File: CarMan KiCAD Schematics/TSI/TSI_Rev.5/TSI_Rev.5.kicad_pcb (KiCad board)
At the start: 2 copper layers, 203.2 x 165.1 mm, 266 parts, among them IC1 TS431ILT, IC4 TS431ILT, J1 TSV, J10 Breakered GLV, J11 Dashboard/EPAL, J12 Battery Packs SL, J13 RSP Safety Loop, J14.1 Logic Conn. 1, J14.2 Logic Conn. 2, J15 Roll Hoop TSAL, J16 Throttle Plau., J17 Brakes & BOT SL, J18 RTDS & Brk Light, J19 Cooling Sensors, J2 Current_Sensor, J20 IMD & AMS BTN, J21 Left Test Conn., J22 Right Side Conn., J23 I2C, J24 MC+ Short Pin 1, J25 MC+ Short Pin 2, J26 HV+ Short Pin 1, J27 HV+ Short Pin 2, J28 HV- Short Pin 1, J29 HV- Short Pin 2, J3 MC, J30 GLV Hook-up Pin, J31 Cooling Jumper, J4 PC Relay, J5 DC Relay, J6 IMD, J7 BP Can & Power, J8 Cockpit, J9 Cooling Power, K1 APAN3105, K2 G5LE-1-E, K3 SFS2-DC24V, K4 SFS2-DC24V, Q1 ZVP1320F, Q11 TN2130K1-G, Q2 MMBF170, Q3 ZVP1320F, Q5 SI1302DL-T1-E3, SW1 TS5A3159DBVT, U1 RDE03110S12, U10 MC7805BDTRKG, U11 TLP293, U12 REF3033, U13 TLP293, U14 Bottom Left, U15 Top Left, U16 TS372CDT, U17 Top Right, U18 MCP6004, U19 74HC00, U2 Bottom Right, U20 TLP293, U21 MCP6004, U22 MCP23016-I_SO, U23 DAC5574IDGS, U24 TLP293, U25 NCD9830DBR2G, U26 MCP6004, U29 SN74LVC1G08DCKR, U3 TS912, U30 TLP293, U31 TLP293, U32 TLP293, U34 TLP293, U35 MCP6004, U37 TLP293, U4 ACPL-C870, U40 MCP6004, U41 PDQ10-Q24-D5-D, U42 LT1763CS8-3.3PBF, U48 TLP293, U49 TLP293, U5 SI8600AB-B-IS, U6 TS912, U7 MCP6004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

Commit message: Updated Brake_Pressed_uC Signal
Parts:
- added R98: 1k, Resistor_SMD:R_0805_2012Metric_Pad1.15x1.40mm_HandSolder, F.Cu at (200.7, 40.6)
- added TP15: SL1_IMD_Out, TestPoint:TestPoint_Pad_D3.0mm, F.Cu at (157.0, 46.5)
- added TP16: SL1_AMS_Out, TestPoint:TestPoint_Pad_D3.0mm, F.Cu at (162.0, 46.5)
- C13: footprint Capacitor_SMD:CP_Elec_10x10 -> Capacitor_THT:CP_Radial_D8.0mm_P3.50mm
- moved C13 0.66 mm to (124.4, 137.2)
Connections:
- U30 pad 3: /AIRS- -> /Throttle_Plausibility/Brake_Pressed_uC
- U30 pad 4: /Throttle_Plausibility/Brake_Pressed_uC -> /Throttle_Plausibility/3.3V

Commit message: TSI Updated & error fixes: added pull down resistors, and 5V_ISO_RTN
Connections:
- IC1 pad 1: Net-(IC1-Pad1) -> (no net)
- IC1 pad 2: Net-(IC1-Pad2) -> (no net)
- IC4 pad 1: Net-(IC4-Pad1) -> (no net)
- IC4 pad 2: Net-(IC4-Pad2) -> (no net)
- J11 pad 8: Net-(J11-Pad8) -> (no net)
- J13 pad 4: Net-(J13-Pad4) -> (no net)
- J2 pad 1: Net-(J2-Pad1) -> (no net)
- J2 pad 6: Net-(J2-Pad6) -> (no net)
- J3 pad 4: Net-(J3-Pad4) -> (no net)
- J6 pad 6: Net-(J6-Pad6) -> (no net)
- J6 pad 7: Net-(J6-Pad7) -> (no net)
- J8 pad 4: Net-(J8-Pad4) -> (no net)
- K2 pad 3: Net-(K2-Pad3) -> (no net)
- K3 pad 3: Net-(K3-Pad3) -> (no net)
- K3 pad 4: Net-(K3-Pad4) -> (no net)
- K4 pad 3: Net-(K4-Pad3) -> (no net)
- K4 pad 4: Net-(K4-Pad4) -> (no net)
- PS1 pad 4: Net-(PS1-Pad4) -> (no net)
- PS1 pad 6: Net-(PS1-Pad6) -> (no net)
- PS2 pad 5: Net-(PS2-Pad5) -> (no net)
- PS2 pad 6: Net-(PS2-Pad6) -> (no net)
- PS2 pad 7: Net-(PS2-Pad7) -> (no net)
- R83 pad 2: /Relays_Cooling_Voltage_Refs/MRSET_Contact -> (no net)
- RV5 pad 3: Net-(RV5-Pad3) -> (no net)
- U22 pad 26: Net-(U22-Pad26) -> (no net)
- U22 pad 27: Net-(U22-Pad27) -> (no net)
- U22 pad 28: Net-(U22-Pad28) -> (no net)
- U22 pad 6: Net-(U22-Pad6) -> (no net)
- U23 pad 2: Net-(U23-Pad2) -> (no net)
- U23 pad 4: Net-(U23-Pad4) -> (no net)
- U23 pad 5: Net-(U23-Pad5) -> (no net)
- U25 pad 1: Net-(U25-Pad1) -> (no net)
- U25 pad 2: Net-(U25-Pad2) -> (no net)
- U25 pad 3: Net-(U25-Pad3) -> (no net)
- U25 pad 6: Net-(U25-Pad6) -> (no net)
- U30 pad 4: /Throttle_Plausibility/3.3V -> (no net)
- U41 pad 6: Net-(U41-Pad6) -> (no net)
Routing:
- net /24V_BP_Out: track 75.4 -> 0.00 mm
- net /SL1_In: track 133.5 -> 105.5 mm
- net /AIRS+: track 96.8 -> 123.7 mm
- net /AIRS-: track 347.7 -> 321.9 mm
- net /IMD_Status: track 231.6 -> 208.2 mm
- net /Throttle_HV: track 137.1 -> 121.0 mm
- net /24V: track 800.3 -> 787.6 mm
- net /BRAKE_OUT: track 218.5 -> 208.4 mm
- net /Gen_Fault_EPAL: track 145.3 -> 137.3 mm
- net /Relays_Cooling_Voltage_Refs/SR_CTRL_Boosted: track 72.2 -> 67.0 mm
- net /Drive_BTN: track 92.1 -> 88.6 mm
- net /BOT_Out: track 66.5 -> 63.5 mm
- net Net-(J3-Pad7): track 29.3 -> 26.9 mm
- net /Brake_Pressed_HV: track 42.8 -> 40.4 mm
- net /5V: track 541.8 -> 540.0 mm
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
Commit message: Updated D2 Footprint
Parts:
- added R99: 1K, Resistor_SMD:R_0805_2012Metric_Pad1.15x1.40mm_HandSolder, F.Cu at (141.2, 41.9)
- D2: footprint Package_SO:MSOP-8_3x3mm_P0.65mm -> Package_SO:SO-8_5.3x6.2mm_P1.27mm
- R61: value 960 -> 1K
- R98: value 1k -> 1K
- moved D1 155.0 mm to (136.4, 41.9)
- moved D4 148.9 mm to (149.9, 41.9), turned to 0 degrees
- moved D2 34.4 mm to (125.7, 45.7)
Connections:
- U11 pad 2: /AIRS- -> /5V_ISO_RTN
- U13 pad 2: /AIRS- -> /5V_ISO_RTN
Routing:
- net Net-(Q2-Pad3): track 134.9 -> 122.4 mm
- net /AIRS-: track 321.9 -> 312.1 mm
- net /Throttle_Plausibility/APPS2_b: track 100.4 -> 95.0 mm, vias 7 -> 6

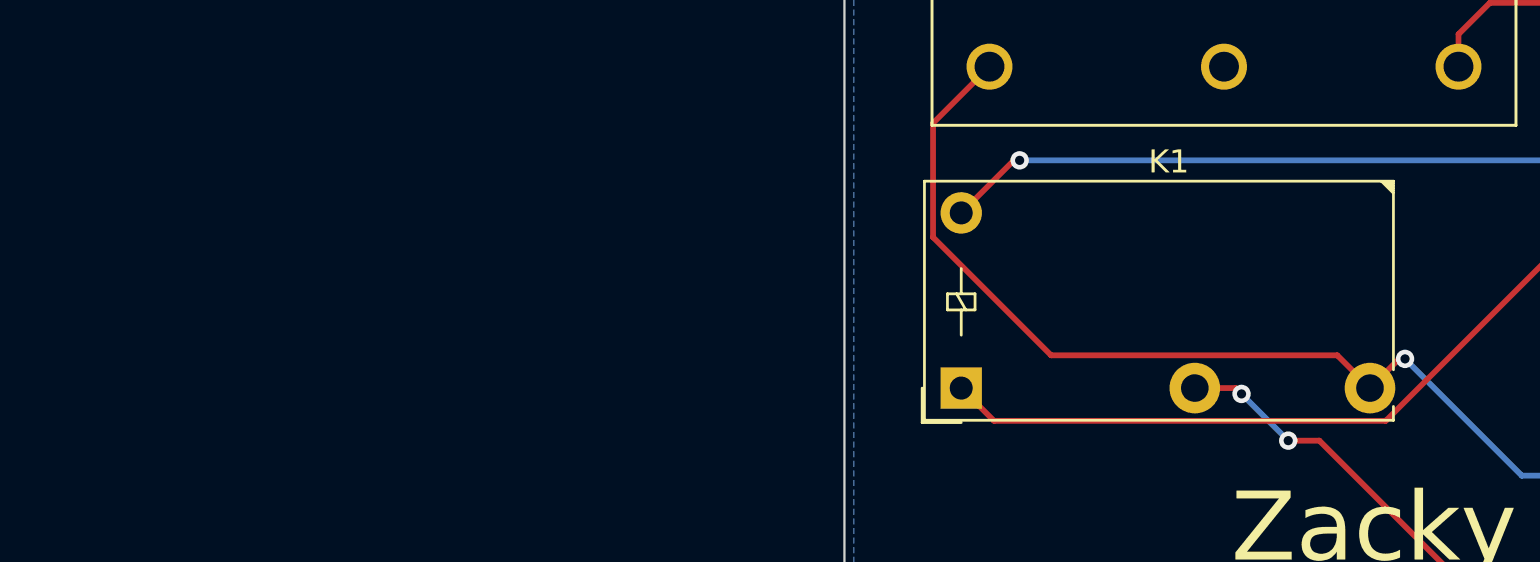
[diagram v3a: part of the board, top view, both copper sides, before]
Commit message: ADDED K1-APAN3105 Relay to symbol and footprint libraries
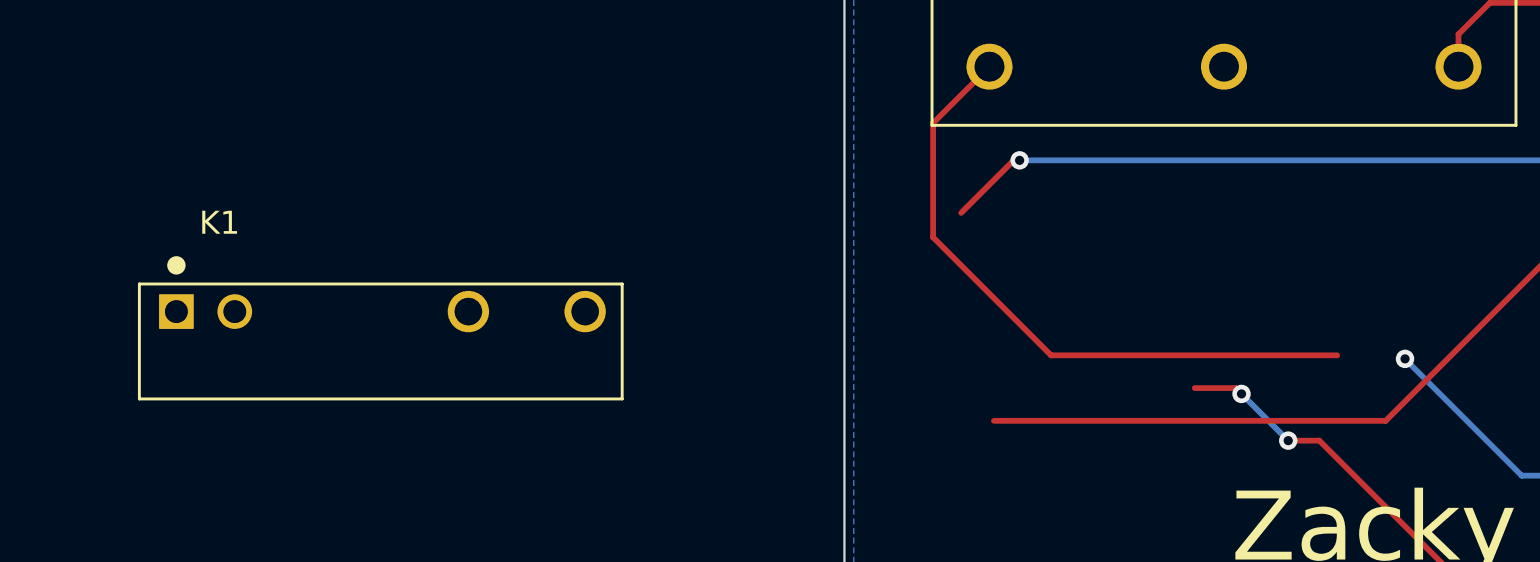
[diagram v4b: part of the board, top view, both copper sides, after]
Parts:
- K1: footprint Relay_THT:Relay_SPST_Finder_32.21-x300 -> TSI_Rev_2021_Footprint_Lib:RELAY_APAN3105
- R65: value 10K -> 2K
- moved K1 34.3 mm to (71.1, 188.0)
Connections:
- IC1 pad 1: (no net) -> Net-(IC1-Pad1)
- IC1 pad 2: (no net) -> Net-(IC1-Pad2)
- IC4 pad 1: (no net) -> Net-(IC4-Pad1)
- IC4 pad 2: (no net) -> Net-(IC4-Pad2)
- J11 pad 8: (no net) -> Net-(J11-Pad8)
- J13 pad 4: (no net) -> Net-(J13-Pad4)
- J2 pad 1: (no net) -> Net-(J2-Pad1)
- J2 pad 6: (no net) -> Net-(J2-Pad6)
- J3 pad 4: (no net) -> Net-(J3-Pad4)
- J6 pad 6: (no net) -> Net-(J6-Pad6)
- J6 pad 7: (no net) -> Net-(J6-Pad7)
- J8 pad 4: (no net) -> Net-(J8-Pad4)
- K2 pad 3: (no net) -> Net-(K2-Pad3)
- K3 pad 3: (no net) -> Net-(K3-Pad3)
- K3 pad 4: (no net) -> Net-(K3-Pad4)
- K4 pad 3: (no net) -> Net-(K4-Pad3)
- K4 pad 4: (no net) -> Net-(K4-Pad4)
- PS1 pad 4: (no net) -> Net-(PS1-Pad4)
- PS1 pad 6: (no net) -> Net-(PS1-Pad6)
- PS2 pad 5: (no net) -> Net-(PS2-Pad5)
- PS2 pad 6: (no net) -> Net-(PS2-Pad6)
- PS2 pad 7: (no net) -> Net-(PS2-Pad7)
- R83 pad 2: (no net) -> /Relays_Cooling_Voltage_Refs/MRSET_Contact
- RV5 pad 3: (no net) -> Net-(RV5-Pad3)
- U22 pad 26: (no net) -> Net-(U22-Pad26)
- U22 pad 27: (no net) -> Net-(U22-Pad27)
- U22 pad 28: (no net) -> Net-(U22-Pad28)
- U22 pad 6: (no net) -> Net-(U22-Pad6)
- U23 pad 2: (no net) -> Net-(U23-Pad2)
- U23 pad 4: (no net) -> Net-(U23-Pad4)
- U23 pad 5: (no net) -> Net-(U23-Pad5)
- U25 pad 1: (no net) -> Net-(U25-Pad1)
- U25 pad 2: (no net) -> Net-(U25-Pad2)
- U25 pad 3: (no net) -> Net-(U25-Pad3)
- U25 pad 6: (no net) -> Net-(U25-Pad6)
- U30 pad 4: (no net) -> /Throttle_Plausibility/3.3V
- U41 pad 6: (no net) -> Net-(U41-Pad6)
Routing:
- net /IGNI_VCC: track 23.7 -> 0.00 mm, vias 2 -> 0
- net (no net): track 0.00 -> 23.7 mm, vias 0 -> 2
- net /PC_RELAY+: track 156.7 -> 152.9 mm
- net /5HV: track 308.8 -> 306.8 mm

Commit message: Updated parts U19 & U12 to have their actual names so we can order them in the future
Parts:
- U19: value 74HC00 -> SN74HC00APWR

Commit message: - removed testing headers (All pins were easily testable, one that weren't received testing points) - Added pull up resistor at drain of SCADA Relay - Fixed issue with U27-PC_Ready signal not being isolated, also added pull down resistor. Comment about 5V_ISO from logic is necessary - Increased Resistor values across D1 and D4 to cut intensity - Updated PCB board with Netlist
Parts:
- removed J22: Right Side Conn., Connector_PinSocket_2.54mm:PinSocket_1x04_P2.54mm_Vertical
- removed J23: I2C, Connector_PinSocket_2.54mm:PinSocket_1x02_P2.54mm_Vertical
- removed R54: 2.4K, Resistor_SMD:R_0805_2012Metric_Pad1.15x1.40mm_HandSolder
- removed U32: TLP293, Package_SO:SOIC-4_4.55x2.6mm_P1.27mm
- added R100: 5K, Resistor_SMD:R_0805_2012Metric_Pad1.15x1.40mm_HandSolder, F.Cu at (63.6, 51.8)
- added R102: 2.4K, Resistor_SMD:R_0805_2012Metric_Pad1.15x1.40mm_HandSolder, F.Cu at (59.1, 55.9)
- added TP17: Throttle Plaus. TP, TestPoint:TestPoint_Pad_D3.0mm, F.Cu at (72.2, 52.8)
- added TP18: Pedal Out, TestPoint:TestPoint_Pad_D3.0mm, F.Cu at (77.2, 52.8)
- added U27: TLP293, Package_SO:SOIC-4_4.55x2.6mm_P1.27mm, F.Cu at (56.4, 52.4)
- J21: value Left Test Conn. -> I2C
- R1: value 76K -> 1K
- R3: value 330 -> 1K
- R38: value 499 -> 1K
- R61: value 1K -> 1.5K
- moved U29 213.5 mm to (54.4, 56.3), turned to 0 degrees
- moved R33 139.3 mm to (53.9, 63.3), turned to 0 degrees
- moved J21 137.6 mm to (104.8, 69.9)
- moved J12 106.8 mm to (312.4, 67.3)
- moved J20 87.4 mm to (53.3, 128.3)
- moved Q11 70.7 mm to (348.0, 128.3)
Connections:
- IC1 pad 1: Net-(IC1-Pad1) -> (no net)
- IC1 pad 2: Net-(IC1-Pad2) -> (no net)
- IC4 pad 1: Net-(IC4-Pad1) -> (no net)
- IC4 pad 2: Net-(IC4-Pad2) -> (no net)
- J11 pad 8: Net-(J11-Pad8) -> (no net)
- J13 pad 4: Net-(J13-Pad4) -> (no net)
- J2 pad 1: Net-(J2-Pad1) -> (no net)
- J2 pad 6: Net-(J2-Pad6) -> (no net)
- J21 pad 1: /SL1_In -> /SDA
- J21 pad 2: /TSAL -> /SCL
- J21 pad 3: /IMD_Status -> /5V
- J21 pad 4: /Throttle_SEL -> /AIRS-
- J3 pad 4: Net-(J3-Pad4) -> (no net)
- J6 pad 6: Net-(J6-Pad6) -> (no net)
- J6 pad 7: Net-(J6-Pad7) -> (no net)
- J8 pad 4: Net-(J8-Pad4) -> (no net)
- K2 pad 3: Net-(K2-Pad3) -> (no net)
- K3 pad 3: Net-(K3-Pad3) -> (no net)
- K3 pad 4: Net-(K3-Pad4) -> (no net)
- K4 pad 3: Net-(K4-Pad3) -> (no net)
- K4 pad 4: Net-(K4-Pad4) -> (no net)
- PS1 pad 4: Net-(PS1-Pad4) -> (no net)
- PS1 pad 6: Net-(PS1-Pad6) -> (no net)
- PS2 pad 5: Net-(PS2-Pad5) -> (no net)
- PS2 pad 6: Net-(PS2-Pad6) -> (no net)
- PS2 pad 7: Net-(PS2-Pad7) -> (no net)
- R33 pad 1: /5V -> /24V
- R33 pad 2: /PC_Ready -> Net-(D3-Pad2)
- R83 pad 2: /Relays_Cooling_Voltage_Refs/MRSET_Contact -> (no net)
- RV5 pad 3: Net-(RV5-Pad3) -> (no net)
- U22 pad 26: Net-(U22-Pad26) -> (no net)
- U22 pad 27: Net-(U22-Pad27) -> (no net)
- U22 pad 28: Net-(U22-Pad28) -> (no net)
- U22 pad 6: Net-(U22-Pad6) -> (no net)
- U23 pad 2: Net-(U23-Pad2) -> (no net)
- U23 pad 4: Net-(U23-Pad4) -> (no net)
- U23 pad 5: Net-(U23-Pad5) -> (no net)
- U25 pad 1: Net-(U25-Pad1) -> (no net)
- U25 pad 2: Net-(U25-Pad2) -> (no net)
- U25 pad 3: Net-(U25-Pad3) -> (no net)
- U25 pad 6: Net-(U25-Pad6) -> (no net)
- U30 pad 4: /Throttle_Plausibility/3.3V -> (no net)
- U41 pad 6: Net-(U41-Pad6) -> (no net)
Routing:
- net /IMD_Button_RTN: track 57.5 -> 29.7 mm
- net /AIRS+: track 123.7 -> 96.8 mm
- net /24V: track 787.6 -> 765.8 mm
- net Net-(Q2-Pad3): track 122.4 -> 100.6 mm
- net /TSAL: track 360.5 -> 340.9 mm
- net /Throttle_SEL: track 212.3 -> 199.5 mm
- net /3.3V: track 230.3 -> 220.9 mm
- net /SL1_In: track 105.5 -> 97.1 mm, vias 3 -> 2
- net /SL1_Out: track 135.9 -> 128.7 mm
- net /AMS_Button_RTN: track 4.97 -> 0.00 mm, vias 1 -> 0
- net /AIRS-: track 312.1 -> 308.1 mm
- net Net-(D3-Pad2): track 6.06 -> 3.79 mm

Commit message: - Removed pull up resistor  - Changed the relay leds such that they are the ones logic and GLV Bob use
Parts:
- removed R33: 5K, Resistor_SMD:R_0805_2012Metric_Pad1.15x1.40mm_HandSolder
- D10, D5, D9: value SML-D13FWT86C -> LED; footprint LED_SMD:LED_0603_1608Metric -> LED_SMD:LED_0805_2012Metric_Pad1.15x1.40mm_HandSolder
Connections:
- U30 pad 4: (no net) -> /3.3V

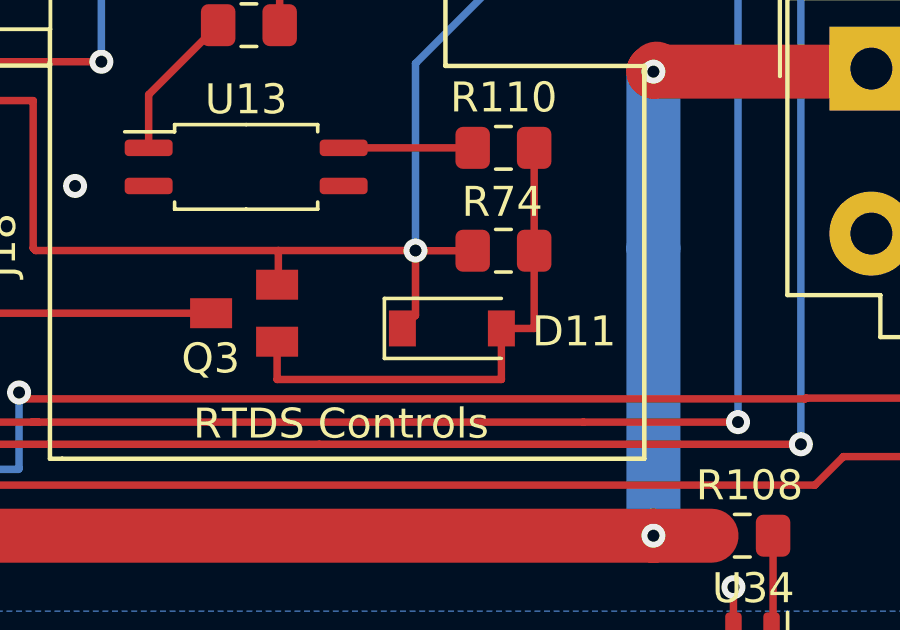
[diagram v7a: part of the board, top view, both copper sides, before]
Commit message: Removed D11 (RTDS Zener diode), made RTDS sound warbled and trash
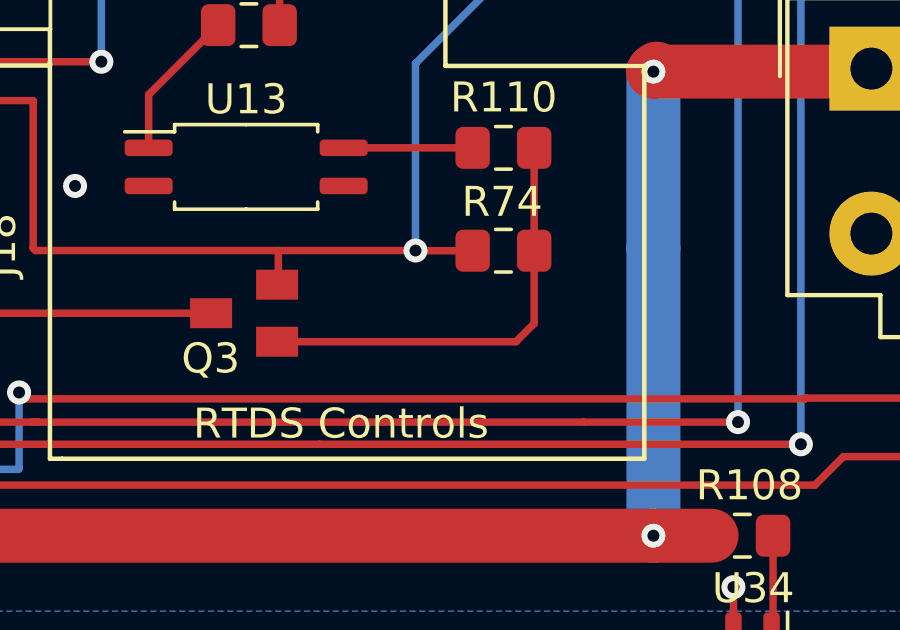
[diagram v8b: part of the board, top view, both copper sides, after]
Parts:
- removed D11: MMSZ5231B-7-F, Diode_SMD:D_SOD-123
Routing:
- net Net-(Q3-Pad1): track 17.5 -> 14.7 mm
- net /24V: track 765.8 -> 763.1 mm
